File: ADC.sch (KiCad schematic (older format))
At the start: 4 parts

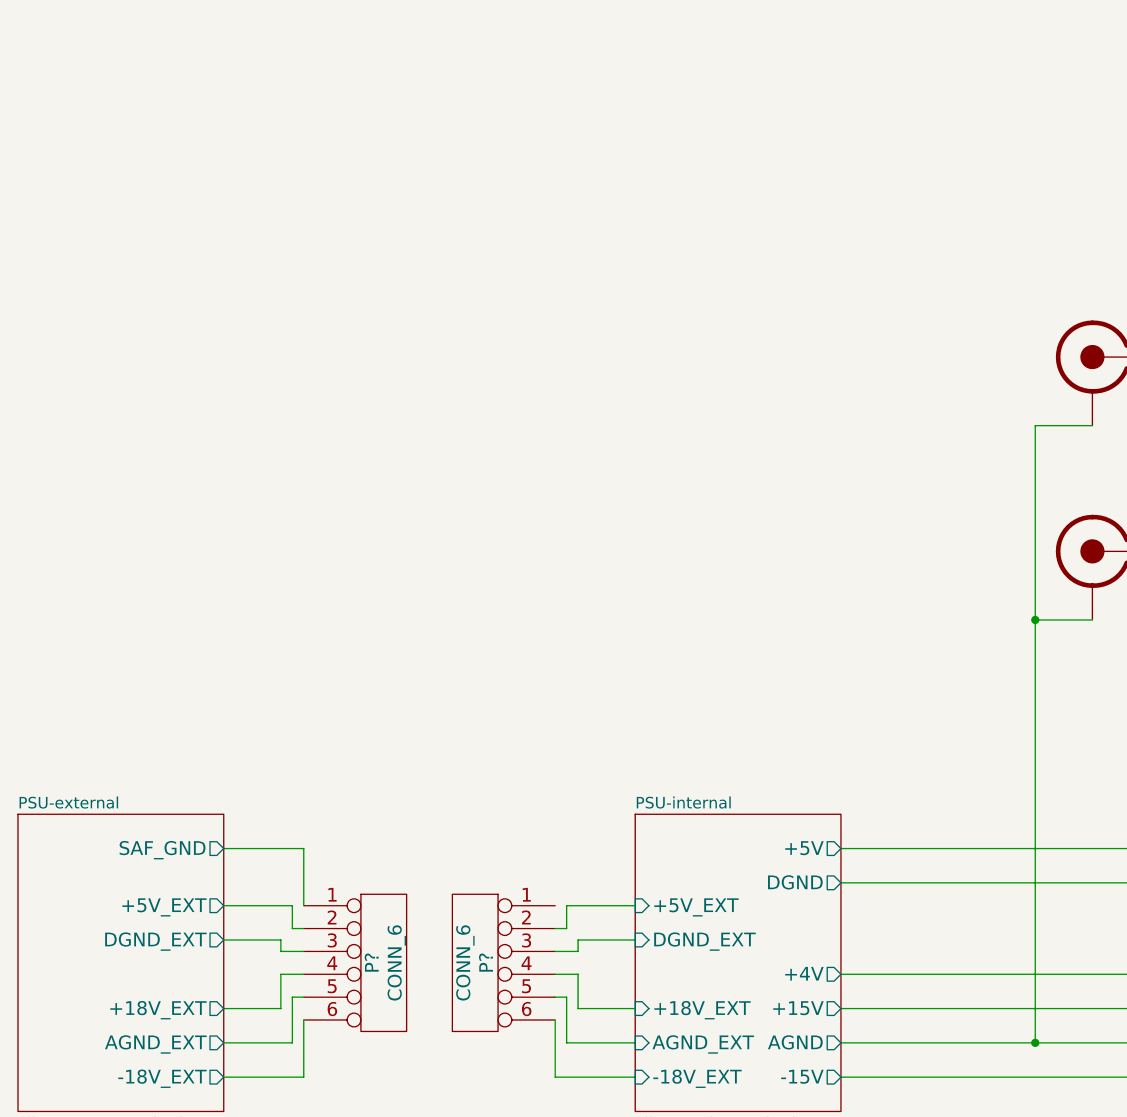
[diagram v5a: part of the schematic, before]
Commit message: Further PSU tweaking for extra safety, added a TODO list.
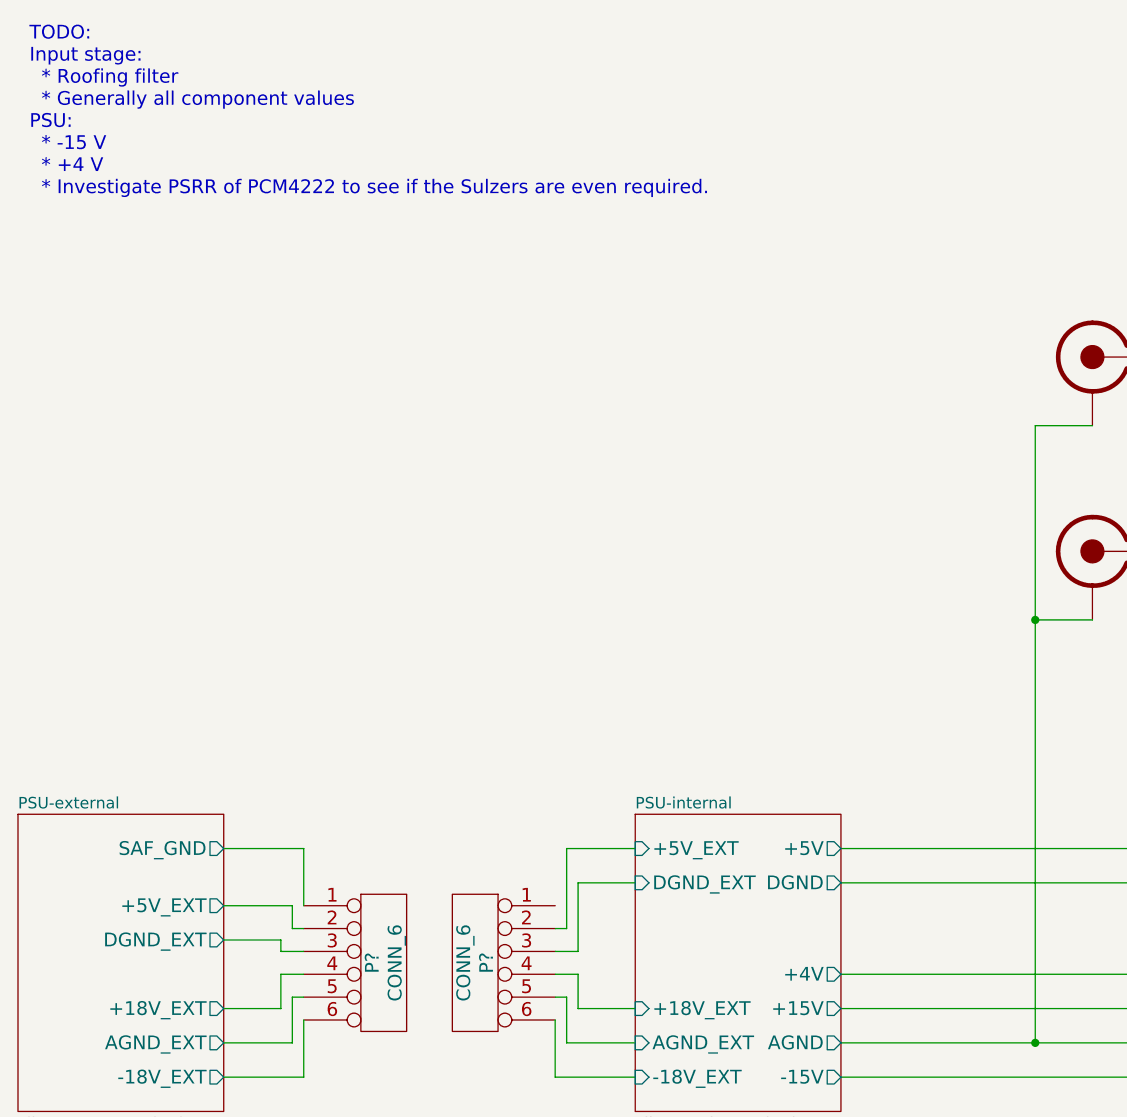
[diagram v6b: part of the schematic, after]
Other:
- note added: "TODO:\nInput stage:\n * Roofing filter\n * Generally all component values\nPSU:\n * -15 V\n * +4 V\n * Investigate PSRR of PCM4222 to see if the Sulzers are even required.\n"
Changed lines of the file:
@@
 F0 "PSU-internal" 50
 F1 "PSU-internal.sch" 50
-F2 "+5V_EXT" I L 3600 4300 60
-F3 "DGND_EXT" I L 3600 4450 60
+F2 "+5V_EXT" I L 3600 4050 60
+F3 "DGND_EXT" I L 3600 4200 60
 F4 "+18V_EXT" I L 3600 4750 60
 F5 "AGND_EXT" I L 3600 4900 60
@@
 	-1   0    0    -1
 $EndComp
-Wire Wire Line
-	1800 4050 2150 4050
-Wire Wire Line
-	2150 4050 2150 4300
-Wire Wire Line
-	1800 4300 2100 4300
-Wire Wire Line
-	2100 4300 2100 4400
-Wire Wire Line
-	2100 4400 2150 4400
-Wire Wire Line
-	1800 4450 2050 4450
-Wire Wire Line
-	2050 4450 2050 4500
-Wire Wire Line
-	2050 4500 2150 4500
-Wire Wire Line
-	1800 4750 2050 4750
-Wire Wire Line
-	2050 4750 2050 4600
-Wire Wire Line
-	2050 4600 2150 4600
-Wire Wire Line
-	1800 4900 2100 4900
-Wire Wire Line
-	2100 4900 2100 4700
-Wire Wire Line
-	2100 4700 2150 4700
-Wire Wire Line
-	1800 5050 2150 5050
-Wire Wire Line
-	2150 5050 2150 4800
-Wire Wire Line
-	3250 4800 3250 5050
-Wire Wire Line
-	3300 4900 3300 4700
-Wire Wire Line
-	3300 4700 3250 4700
-Wire Wire Line
-	3250 4600 3350 4600
-Wire Wire Line
-	3350 4600 3350 4750
-Wire Wire Line
-	3350 4450 3350 4500
-Wire Wire Line
-	3350 4500 3250 4500
-Wire Wire Line
-	3250 4400 3300 4400
-Wire Wire Line
-	3300 4400 3300 4300
-Wire Wire Line
-	3300 4300 3600 4300
-Wire Wire Line
-	3600 4450 3350 4450
-Wire Wire Line
-	3350 4750 3600 4750
-Wire Wire Line
-	3600 4900 3300 4900
-Wire Wire Line
-	3250 5050 3600 5050
 $Sheet
 S 6450 2200 900  1200
@@
 F8 "LOUT" O R 8850 2350 60
 $EndSheet
-Wire Wire Line
-	6450 3250 6350 3250
-Wire Wire Line
-	6350 3250 6350 5050
-Wire Wire Line
-	6450 3100 6250 3100
-Wire Wire Line
-	6250 3100 6250 4900
-Wire Wire Line
-	6450 2950 6150 2950
-Wire Wire Line
-	6150 2950 6150 4750
-Wire Wire Line
-	7950 2950 7650 2950
-Wire Wire Line
-	7650 2950 7650 4750
-Connection ~ 6150 4750
-Wire Wire Line
-	7950 3100 7750 3100
-Wire Wire Line
-	7750 3100 7750 4900
-Connection ~ 6250 4900
-Wire Wire Line
-	7950 3250 7850 3250
-Wire Wire Line
-	7850 3250 7850 5050
-Connection ~ 6350 5050
-Wire Wire Line
-	7350 2350 7950 2350
-Wire Wire Line
-	7950 2550 7350 2550
 $Sheet
 S 9650 2200 1100 3000
@@
 F11 "RIN+" I L 9650 2950 60
 $EndSheet
-Wire Wire Line
-	9650 2350 8850 2350
-Wire Wire Line
-	8850 2550 9650 2550
-Connection ~ 7650 4750
-Connection ~ 7750 4900
-Connection ~ 7850 5050
-Wire Wire Line
-	9650 2750 9350 2750
-Wire Wire Line
-	9350 2750 9350 4900
-Connection ~ 9350 4900
-Wire Wire Line
-	9350 2950 9650 2950
-Connection ~ 9350 2950
 $Comp
 L RCA J?
@@
 $EndComp
 Wire Wire Line
+	1800 4050 2150 4050
+Wire Wire Line
+	2150 4050 2150 4300
+Wire Wire Line
+	1800 4300 2100 4300
+Wire Wire Line
+	2100 4300 2100 4400
+Wire Wire Line
+	2100 4400 2150 4400
+Wire Wire Line
+	1800 4450 2050 4450
+Wire Wire Line
+	2050 4450 2050 4500
+Wire Wire Line
+	2050 4500 2150 4500
+Wire Wire Line
+	1800 4750 2050 4750
+Wire Wire Line
+	2050 4750 2050 4600
+Wire Wire Line
+	2050 4600 2150 4600
+Wire Wire Line
+	1800 4900 2100 4900
+Wire Wire Line
+	2100 4900 2100 4700
+Wire Wire Line
+	2100 4700 2150 4700
+Wire Wire Line
+	1800 5050 2150 5050
+Wire Wire Line
+	2150 5050 2150 4800
+Wire Wire Line
+	3250 4800 3250 5050
+Wire Wire Line
+	3300 4900 3300 4700
+Wire Wire Line
+	3300 4700 3250 4700
+Wire Wire Line
+	3250 4600 3350 4600
+Wire Wire Line
+	3350 4600 3350 4750
+Wire Wire Line
+	3350 4200 3350 4500
+Wire Wire Line
+	3350 4500 3250 4500
+Wire Wire Line
+	3300 4400 3250 4400
+Wire Wire Line
+	3300 4050 3300 4400
+Wire Wire Line
+	3350 4750 3600 4750
+Wire Wire Line
+	3600 4900 3300 4900
+Wire Wire Line
+	3250 5050 3600 5050
+Wire Wire Line
+	6450 3250 6350 3250
+Wire Wire Line
+	6350 3250 6350 5050
+Wire Wire Line
+	6450 3100 6250 3100
+Wire Wire Line
+	6250 3100 6250 4900
+Wire Wire Line
+	6450 2950 6150 2950
+Wire Wire Line
+	6150 2950 6150 4750
+Wire Wire Line
+	7950 2950 7650 2950
+Wire Wire Line
+	7650 2950 7650 4750
+Connection ~ 6150 4750
+Wire Wire Line
+	7950 3100 7750 3100
+Wire Wire Line
+	7750 3100 7750 4900
+Connection ~ 6250 4900
+Wire Wire Line
+	7950 3250 7850 3250
+Wire Wire Line
+	7850 3250 7850 5050
+Connection ~ 6350 5050
+Wire Wire Line
+	7350 2350 7950 2350
+Wire Wire Line
+	7950 2550 7350 2550
+Wire Wire Line
+	9650 2350 8850 2350
+Wire Wire Line
+	8850 2550 9650 2550
+Connection ~ 7650 4750
+Connection ~ 7750 4900
+Connection ~ 7850 5050
+Wire Wire Line
+	9650 2750 9350 2750
+Wire Wire Line
+	9350 2750 9350 4900
+Connection ~ 9350 4900
+Wire Wire Line
+	9350 2950 9650 2950
+Connection ~ 9350 2950
+Wire Wire Line
 	5600 2200 5350 2200
 Wire Wire Line
@@
 Wire Wire Line
 	9650 5050 4500 5050
+Wire Wire Line
+	3600 4200 3350 4200
+Wire Wire Line
+	3300 4050 3600 4050
+Text Notes 950  1200 0    60   ~ 0
+TODO:\nInput stage:\n  * Roofing filter\n  * Generally all component values\nPSU:\n  * -15 V\n  * +4 V\n  * Investigate PSRR of PCM4222 to see if the Sulzers are even required.\n
 $EndSCHEMATC
